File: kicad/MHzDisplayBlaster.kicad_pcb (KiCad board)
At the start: 2 copper layers, 50 x 39 mm, 7 parts, among them J1 Conn_02x15 DigitLHS, J2 Conn_02x15 DigitRHS, J3 Conn_01x03_Pin, U1 DC56-11GWA, U2 74LS04

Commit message: Fix missing routes on 7404
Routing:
- net 1: track 149.2 -> 157.6 mm
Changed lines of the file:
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@@
   (segment (start 103.44 76.54) (end 104.615 77.715) (width 0.25) (layer "B.Cu") (net 1))
   (segment (start 102.953299 41.825) (end 102.265 42.513299) (width 0.25) (layer "B.Cu") (net 1))
+  (segment (start 148.75 58.75) (end 148 58) (width 0.25) (layer "B.Cu") (net 1))
   (segment (start 122.585 41.825) (end 114.775 41.825) (width 0.25) (layer "B.Cu") (net 1))
   (segment (start 133.92 76.54) (end 133.92 74) (width 0.25) (layer "B.Cu") (net 1))
   (segment (start 102 47) (end 102 72.56) (width 0.25) (layer "B.Cu") (net 1))
   (segment (start 124.935 41.825) (end 123.76 43) (width 0.25) (layer "B.Cu") (net 1))
+  (segment (start 148.04 60.54) (end 147.45 60.54) (width 0.25) (layer "B.Cu") (net 1))
   (segment (start 133.92 43) (end 133.92 45.54) (width 0.25) (layer "B.Cu") (net 1))
+  (segment (start 148.75 61.25) (end 148.04 60.54) (width 0.25) (layer "B.Cu") (net 1))
   (segment (start 114.775 77.715) (end 122.585 77.715) (width 0.25) (layer "B.Cu") (net 1))
   (segment (start 113.6 43) (end 112.425 41.825) (width 0.25) (layer "B.Cu") (net 1))
   (segment (start 104.615 77.715) (end 112.425 77.715) (width 0.25) (layer "B.Cu") (net 1))
+  (segment (start 147.826751 60.54) (end 148.75 59.616751) (width 0.25) (layer "B.Cu") (net 1))
+  (segment (start 148.75 62.156751) (end 148.75 61.25) (width 0.25) (layer "B.Cu") (net 1))
+  (segment (start 148 58) (end 147.45 58) (width 0.25) (layer "B.Cu") (net 1))
   (segment (start 145 41.5) (end 135.42 41.5) (width 0.25) (layer "B.Cu") (net 1))
   (segment (start 147.45 58) (end 149 56.45) (width 0.25) (layer "B.Cu") (net 1))
@@
   (segment (start 102.265 42.513299) (end 102.265 44.365) (width 0.25) (layer "B.Cu") (net 1))
   (segment (start 103.44 45.56) (end 102 47) (width 0.25) (layer "B.Cu") (net 1))
+  (segment (start 147.45 63.08) (end 147.826751 63.08) (width 0.25) (layer "B.Cu") (net 1))
   (segment (start 133.92 76.54) (end 132.745 77.715) (width 0.25) (layer "B.Cu") (net 1))
+  (segment (start 148.75 59.616751) (end 148.75 58.75) (width 0.25) (layer "B.Cu") (net 1))
   (segment (start 149 56.45) (end 149 45.5) (width 0.25) (layer "B.Cu") (net 1))
   (segment (start 102 72.56) (end 103.44 74) (width 0.25) (layer "B.Cu") (net 1))
@@
   (segment (start 132.745 41.825) (end 124.935 41.825) (width 0.25) (layer "B.Cu") (net 1))
   (segment (start 123.76 43) (end 123.76 45.54) (width 0.25) (layer "B.Cu") (net 1))
+  (segment (start 147.826751 63.08) (end 148.75 62.156751) (width 0.25) (layer "B.Cu") (net 1))
   (segment (start 123.76 43) (end 122.585 41.825) (width 0.25) (layer "B.Cu") (net 1))
+  (segment (start 147.45 60.54) (end 147.826751 60.54) (width 0.25) (layer "B.Cu") (net 1))
   (segment (start 133.92 43) (end 132.745 41.825) (width 0.25) (layer "B.Cu") (net 1))
   (segment (start 123.76 76.54) (end 124.935 77.715) (width 0.25) (layer "B.Cu") (net 1))

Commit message: More trace cleanup
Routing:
- net 1: track 157.6 -> 188.3 mm
- net Turbo: track 19.6 -> 18.1 mm
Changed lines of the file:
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@@
   (segment (start 133.92 43) (end 133.92 45.54) (width 0.25) (layer "B.Cu") (net 1))
   (segment (start 148.75 61.25) (end 148.04 60.54) (width 0.25) (layer "B.Cu") (net 1))
+  (segment (start 147.45 63.08) (end 147.826751 63.08) (width 0.25) (layer "B.Cu") (net 1))
+  (segment (start 147.826751 63.08) (end 149.175 64.428249) (width 0.25) (layer "B.Cu") (net 1))
   (segment (start 114.775 77.715) (end 122.585 77.715) (width 0.25) (layer "B.Cu") (net 1))
   (segment (start 113.6 43) (end 112.425 41.825) (width 0.25) (layer "B.Cu") (net 1))
+  (segment (start 148.785 77.715) (end 135.095 77.715) (width 0.25) (layer "B.Cu") (net 1))
   (segment (start 104.615 77.715) (end 112.425 77.715) (width 0.25) (layer "B.Cu") (net 1))
   (segment (start 147.826751 60.54) (end 148.75 59.616751) (width 0.25) (layer "B.Cu") (net 1))
@@
   (segment (start 148 58) (end 147.45 58) (width 0.25) (layer "B.Cu") (net 1))
   (segment (start 145 41.5) (end 135.42 41.5) (width 0.25) (layer "B.Cu") (net 1))
+  (segment (start 149.175 64.428249) (end 149.175 77.325) (width 0.25) (layer "B.Cu") (net 1))
   (segment (start 147.45 58) (end 149 56.45) (width 0.25) (layer "B.Cu") (net 1))
   (segment (start 103.44 45.54) (end 103.44 45.56) (width 0.25) (layer "B.Cu") (net 1))
@@
   (segment (start 102.265 42.513299) (end 102.265 44.365) (width 0.25) (layer "B.Cu") (net 1))
   (segment (start 103.44 45.56) (end 102 47) (width 0.25) (layer "B.Cu") (net 1))
-  (segment (start 147.45 63.08) (end 147.826751 63.08) (width 0.25) (layer "B.Cu") (net 1))
   (segment (start 133.92 76.54) (end 132.745 77.715) (width 0.25) (layer "B.Cu") (net 1))
   (segment (start 148.75 59.616751) (end 148.75 58.75) (width 0.25) (layer "B.Cu") (net 1))
+  (segment (start 149.175 77.325) (end 148.785 77.715) (width 0.25) (layer "B.Cu") (net 1))
   (segment (start 149 56.45) (end 149 45.5) (width 0.25) (layer "B.Cu") (net 1))
   (segment (start 102 72.56) (end 103.44 74) (width 0.25) (layer "B.Cu") (net 1))
@@
   (segment (start 123.76 43) (end 122.585 41.825) (width 0.25) (layer "B.Cu") (net 1))
   (segment (start 147.45 60.54) (end 147.826751 60.54) (width 0.25) (layer "B.Cu") (net 1))
+  (segment (start 135.095 77.715) (end 133.92 76.54) (width 0.25) (layer "B.Cu") (net 1))
   (segment (start 133.92 43) (end 132.745 41.825) (width 0.25) (layer "B.Cu") (net 1))
   (segment (start 123.76 76.54) (end 124.935 77.715) (width 0.25) (layer "B.Cu") (net 1))
@@
   (segment (start 138.5 65.82) (end 137.32 67) (width 0.25) (layer "B.Cu") (net 19))
   (segment (start 142.92 68.46) (end 142.46 68) (width 0.25) (layer "B.Cu") (net 20))
-  (segment (start 142.42 65.7) (end 142.5 65.62) (width 0.25) (layer "B.Cu") (net 20))
-  (segment (start 142.46 72.04) (end 142.92 72.5) (width 0.25) (layer "B.Cu") (net 20))
   (segment (start 142.5 65.62) (end 144.38 65.62) (width 0.25) (layer "B.Cu") (net 20))
   (segment (start 144.38 65.62) (end 144.665 65.335) (width 0.25) (layer "B.Cu") (net 20))
@@
   (segment (start 143.87 60.54) (end 142.5 60.54) (width 0.25) (layer "B.Cu") (net 20))
   (segment (start 144.665 65.335) (end 144.665 62.835) (width 0.25) (layer "B.Cu") (net 20))
-  (segment (start 142.46 65.66) (end 142.5 65.62) (width 0.25) (layer "B.Cu") (net 20))
-  (segment (start 142.42 72) (end 142.92 72.5) (width 0.25) (layer "B.Cu") (net 20))
   (segment (start 144.42 63.08) (end 144.665 62.835) (width 0.25) (layer "B.Cu") (net 20))
   (segment (start 142.46 68) (end 142.46 65.66) (width 0.25) (layer "B.Cu") (net 20))

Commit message: Add Graphical Notes
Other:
- board text added: "100"
- board text added: "1k"
- board text added: "ST-6A"

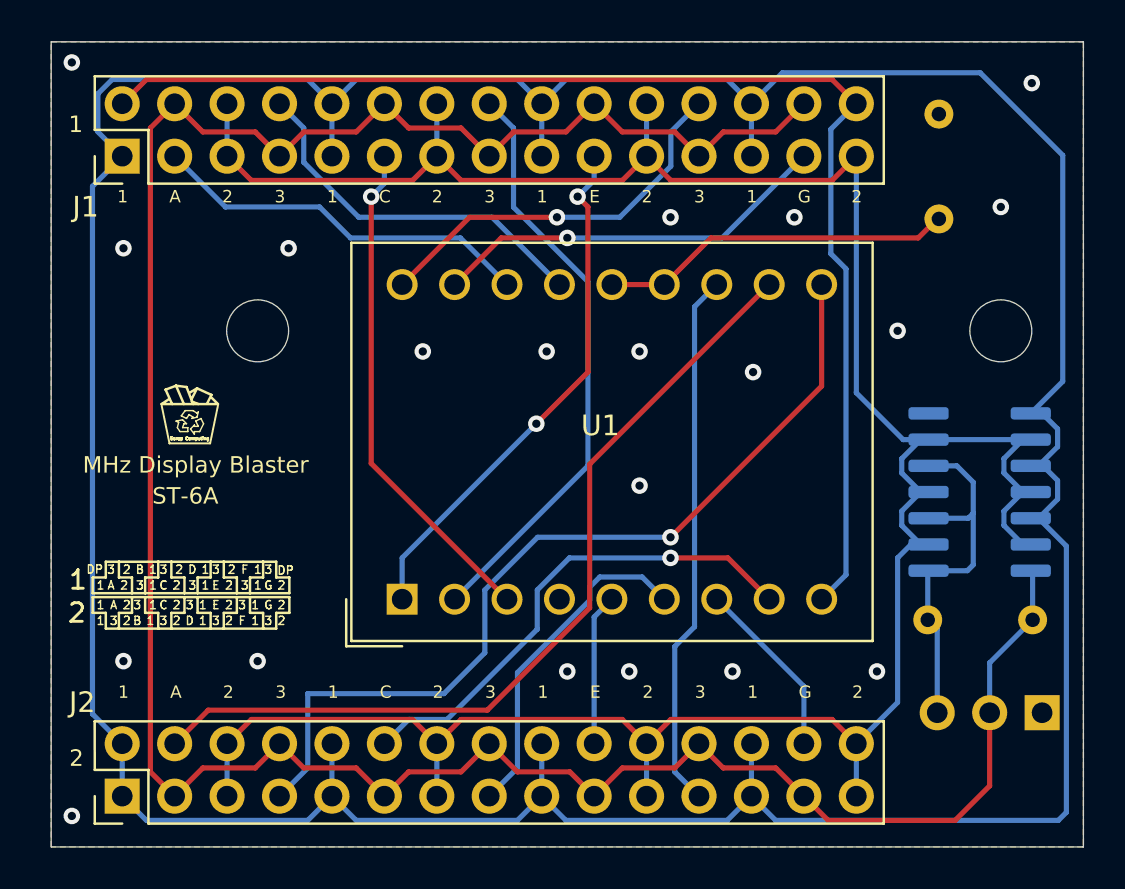
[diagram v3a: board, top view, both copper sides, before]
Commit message: Connect Display pin 4 & Trace Cleanup
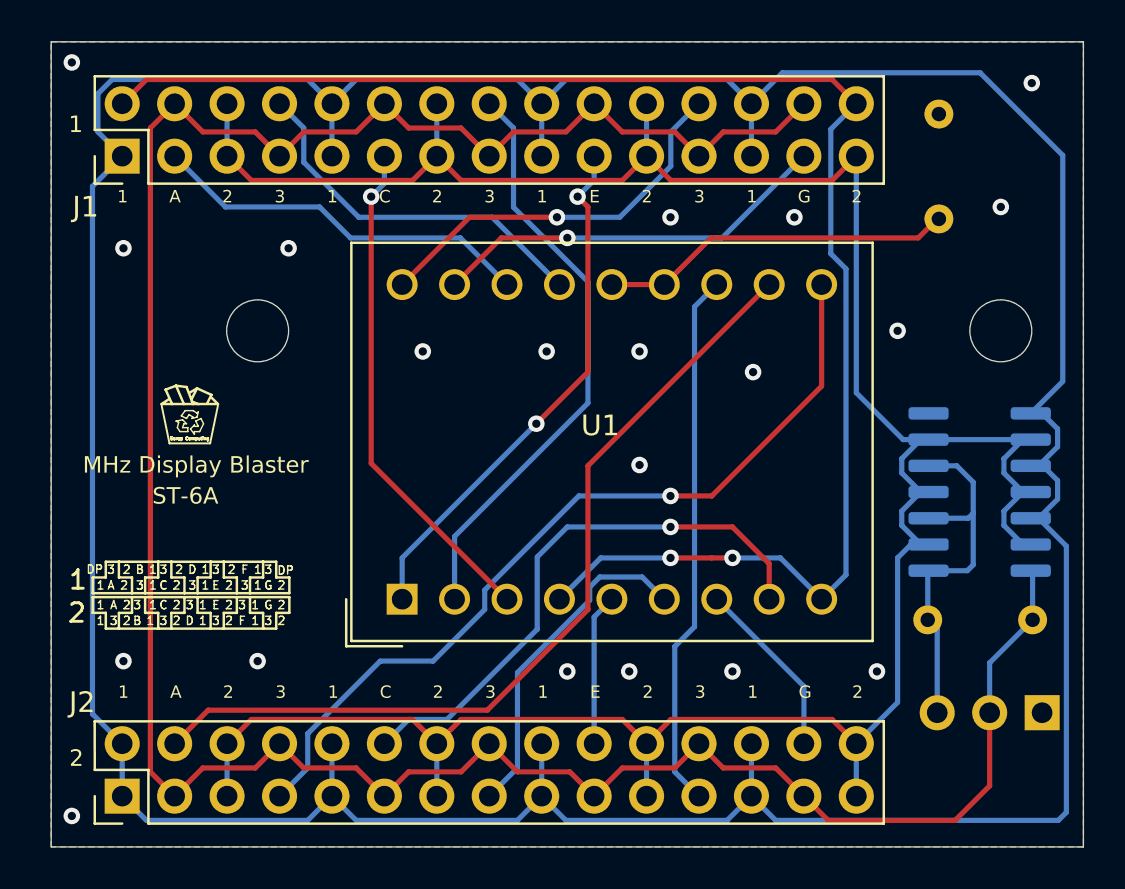
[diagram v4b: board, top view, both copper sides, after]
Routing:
- net DP: track 61.8 -> 76.2 mm, vias 0 -> 2
- net DIG2_C: track 24.3 -> 27.5 mm
- net DIG2_B: track 43.3 -> 40.9 mm
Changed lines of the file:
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@@
   (segment (start 130.015 46.026701) (end 127.541701 48.5) (width 0.25) (layer "B.Cu") (net 8))
   (segment (start 130.015 44.365) (end 130.015 46.026701) (width 0.25) (layer "B.Cu") (net 8))
-  (segment (start 126 60.54) (end 119.54 67) (width 0.25) (layer "B.Cu") (net 9))
+  (segment (start 121.22 43) (end 122.395 44.175) (width 0.25) (layer "B.Cu") (net 9))
+  (segment (start 119.54 63.96) (end 119.54 67) (width 0.25) (layer "B.Cu") (net 9))
+  (segment (start 126 57.5) (end 119.54 63.96) (width 0.25) (layer "B.Cu") (net 9))
+  (segment (start 122.395 44.175) (end 122.395 48.01472) (width 0.25) (layer "B.Cu") (net 9))
   (segment (start 122.395 48.01472) (end 126 51.61972) (width 0.25) (layer "B.Cu") (net 9))
-  (segment (start 121.22 43) (end 122.395 44.175) (width 0.25) (layer "B.Cu") (net 9))
-  (segment (start 122.395 44.175) (end 122.395 48.01472) (width 0.25) (layer "B.Cu") (net 9))
-  (segment (start 126 51.61972) (end 126 60.54) (width 0.25) (layer "B.Cu") (net 9))
+  (segment (start 126 51.61972) (end 126 57.5) (width 0.25) (layer "B.Cu") (net 9))
   (segment (start 112.235 44.175) (end 111.06 43) (width 0.25) (layer "B.Cu") (net 10))
   (segment (start 114.898299 48.5) (end 112.235 45.836701) (width 0.25) (layer "B.Cu") (net 10))
@@
   (segment (start 124.62 51.76) (end 121.36 48.5) (width 0.25) (layer "B.Cu") (net 10))
   (segment (start 121.36 48.5) (end 114.898299 48.5) (width 0.25) (layer "B.Cu") (net 10))
-  (segment (start 130 64) (end 137.32 56.68) (width 0.25) (layer "F.Cu") (net 11))
+  (segment (start 130 62) (end 132 62) (width 0.25) (layer "F.Cu") (net 11))
+  (segment (start 132 62) (end 137.32 56.68) (width 0.25) (layer "F.Cu") (net 11))
   (segment (start 137.32 56.68) (end 137.32 51.76) (width 0.25) (layer "F.Cu") (net 11))
-  (via (at 130 64) (size 0.8) (drill 0.4) (layers "F.Cu" "B.Cu") (net 11))
-  (segment (start 111.06 76.54) (end 112.425 75.175) (width 0.25) (layer "B.Cu") (net 11))
-  (segment (start 119.02528 71.575) (end 121.005 69.59528) (width 0.25) (layer "B.Cu") (net 11))
-  (segment (start 123.55972 64) (end 130 64) (width 0.25) (layer "B.Cu") (net 11))
-  (segment (start 121.005 66.55472) (end 123.55972 64) (width 0.25) (layer "B.Cu") (net 11))
-  (segment (start 112.425 75.175) (end 112.425 71.575) (width 0.25) (layer "B.Cu") (net 11))
-  (segment (start 112.425 71.575) (end 119.02528 71.575) (width 0.25) (layer "B.Cu") (net 11))
-  (segment (start 121.005 69.59528) (end 121.005 66.55472) (width 0.25) (layer "B.Cu") (net 11))
+  (via (at 130 62) (size 0.8) (drill 0.4) (layers "F.Cu" "B.Cu") (net 11))
+  (segment (start 130 62) (end 125.55972 62) (width 0.25) (layer "B.Cu") (net 11))
+  (segment (start 115.938299 70) (end 112.425 73.513299) (width 0.25) (layer "B.Cu") (net 11))
+  (segment (start 121 66.55972) (end 121 67.5) (width 0.25) (layer "B.Cu") (net 11))
+  (segment (start 112.425 73.513299) (end 112.425 75.175) (width 0.25) (layer "B.Cu") (net 11))
+  (segment (start 118.5 70) (end 115.938299 70) (width 0.25) (layer "B.Cu") (net 11))
+  (segment (start 112.425 75.175) (end 111.06 76.54) (width 0.25) (layer "B.Cu") (net 11))
+  (segment (start 121 67.5) (end 118.5 70) (width 0.25) (layer "B.Cu") (net 11))
+  (segment (start 125.55972 62) (end 121 66.55972) (width 0.25) (layer "B.Cu") (net 11))
   (segment (start 122.585 75.175) (end 122.585 70.55528) (width 0.25) (layer "B.Cu") (net 12))
   (segment (start 126.575 65.925) (end 128.625 65.925) (width 0.25) (layer "B.Cu") (net 12))
@@
   (segment (start 126.3 67.86) (end 127.16 67) (width 0.25) (layer "B.Cu") (net 15))
   (segment (start 126.3 74) (end 126.3 67.86) (width 0.25) (layer "B.Cu") (net 15))
-  (segment (start 132.78 65) (end 134.78 67) (width 0.25) (layer "F.Cu") (net 16))
-  (segment (start 130 65) (end 132.78 65) (width 0.25) (layer "F.Cu") (net 16))
-  (via (at 130 65) (size 0.8) (drill 0.4) (layers "F.Cu" "B.Cu") (net 16))
-  (segment (start 116.14 74) (end 117.315 72.825) (width 0.25) (layer "B.Cu") (net 16))
-  (segment (start 117.315 72.825) (end 119.175 72.825) (width 0.25) (layer "B.Cu") (net 16))
-  (segment (start 123.545 68.455) (end 123.545 66.55472) (width 0.25) (layer "B.Cu") (net 16))
-  (segment (start 125.09972 65) (end 130 65) (width 0.25) (layer "B.Cu") (net 16))
-  (segment (start 123.545 66.55472) (end 125.09972 65) (width 0.25) (layer "B.Cu") (net 16))
-  (segment (start 119.175 72.825) (end 123.545 68.455) (width 0.25) (layer "B.Cu") (net 16))
+  (segment (start 133 63.5) (end 134.78 65.28) (width 0.25) (layer "F.Cu") (net 16))
+  (segment (start 134.78 65.28) (end 134.78 67) (width 0.25) (layer "F.Cu") (net 16))
+  (segment (start 130 63.5) (end 133 63.5) (width 0.25) (layer "F.Cu") (net 16))
+  (via (at 130 63.5) (size 0.8) (drill 0.4) (layers "F.Cu" "B.Cu") (net 16))
+  (segment (start 123.545 68.455) (end 119.175 72.825) (width 0.25) (layer "B.Cu") (net 16))
+  (segment (start 119.175 72.825) (end 117.315 72.825) (width 0.25) (layer "B.Cu") (net 16))
+  (segment (start 130 63.5) (end 125 63.5) (width 0.25) (layer "B.Cu") (net 16))
+  (segment (start 123.545 64.955) (end 123.545 68.455) (width 0.25) (layer "B.Cu") (net 16))
+  (segment (start 125 63.5) (end 123.545 64.955) (width 0.25) (layer "B.Cu") (net 16))
+  (segment (start 117.315 72.825) (end 116.14 74) (width 0.25) (layer "B.Cu") (net 16))
+  (segment (start 121.125 72.375) (end 126 67.5) (width 0.25) (layer "F.Cu") (net 17))
+  (segment (start 126 60.54) (end 134.78 51.76) (width 0.25) (layer "F.Cu") (net 17))
+  (segment (start 126 67.5) (end 126 60.54) (width 0.25) (layer "F.Cu") (net 17))
+  (segment (start 105.98 74) (end 107.605 72.375) (width 0.25) (layer "F.Cu") (net 17))
   (segment (start 107.605 72.375) (end 121.125 72.375) (width 0.25) (layer "F.Cu") (net 17))
-  (segment (start 126.085 60.455) (end 134.78 51.76) (width 0.25) (layer "F.Cu") (net 17))
-  (segment (start 121.125 72.375) (end 126.085 67.415) (width 0.25) (layer "F.Cu") (net 17))
-  (segment (start 126.085 67.415) (end 126.085 60.455) (width 0.25) (layer "F.Cu") (net 17))
-  (segment (start 105.98 74) (end 107.605 72.375) (width 0.25) (layer "F.Cu") (net 17))
   (segment (start 131.96 49.5) (end 129.7 51.76) (width 0.25) (layer "F.Cu") (net 18))
   (segment (start 143 48.5) (end 142 49.5) (width 0.25) (layer "F.Cu") (net 18))
@@
   (segment (start 129.7 51.76) (end 127.16 51.76) (width 0.25) (layer "F.Cu") (net 18))
   (segment (start 104.615 41.825) (end 137.825 41.825) (width 0.25) (layer "F.Cu") (net 19))
+  (segment (start 130 65) (end 132 65) (width 0.25) (layer "F.Cu") (net 19))
   (segment (start 103.44 43) (end 104.615 41.825) (width 0.25) (layer "F.Cu") (net 19))
+  (segment (start 132 65) (end 133 65) (width 0.25) (layer "F.Cu") (net 19))
   (segment (start 137.825 41.825) (end 139 43) (width 0.25) (layer "F.Cu") (net 19))
+  (via (at 133 65) (size 0.8) (drill 0.4) (layers "F.Cu" "B.Cu") (net 19))
+  (via (at 130 65) (size 0.8) (drill 0.4) (layers "F.Cu" "B.Cu") (net 19))
+  (segment (start 126.62 65) (end 130 65) (width 0.25) (layer "B.Cu") (net 19))
   (segment (start 137.76528 50.26528) (end 138.5 51) (width 0.25) (layer "B.Cu") (net 19))
   (segment (start 139 43) (end 137.76528 44.23472) (width 0.25) (layer "B.Cu") (net 19))
+  (segment (start 135.32 65) (end 137.32 67) (width 0.25) (layer "B.Cu") (net 19))
   (segment (start 137.76528 44.23472) (end 137.76528 50.26528) (width 0.25) (layer "B.Cu") (net 19))
   (segment (start 138.5 51) (end 138.5 65.82) (width 0.25) (layer "B.Cu") (net 19))
+  (segment (start 133 65) (end 135.32 65) (width 0.25) (layer "B.Cu") (net 19))
   (segment (start 138.5 65.82) (end 137.32 67) (width 0.25) (layer "B.Cu") (net 19))
+  (segment (start 124.62 67) (end 126.62 65) (width 0.25) (layer "B.Cu") (net 19))
   (segment (start 142.92 68.46) (end 142.46 68) (width 0.25) (layer "B.Cu") (net 20))
   (segment (start 142.5 65.62) (end 144.38 65.62) (width 0.25) (layer "B.Cu") (net 20))
@@
   (via (at 133 70.5) (size 0.8) (drill 0.4) (layers "F.Cu" "B.Cu") (free) (net 21))
   (via (at 146 48) (size 0.8) (drill 0.4) (layers "F.Cu" "B.Cu") (free) (net 21))
-  (via (at 128.5 61.5) (size 0.8) (drill 0.4) (layers "F.Cu" "B.Cu") (free) (net 21))
+  (via (at 128.5 60.5) (size 0.8) (drill 0.4) (layers "F.Cu" "B.Cu") (free) (net 21))
   (via (at 103.5 70) (size 0.8) (drill 0.4) (layers "F.Cu" "B.Cu") (free) (net 21))
   (via (at 103.5 50) (size 0.8) (drill 0.4) (layers "F.Cu" "B.Cu") (free) (net 21))
